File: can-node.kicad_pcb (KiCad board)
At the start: 2 copper layers, 50 x 60 mm, 96 parts, among them P1 Debug, P3 CONN_01X04, Q1 DMP6023LSS, Q10 BSS138, Q11 BSS84P, Q12 BSS84P, Q13 BSS84P, Q14 BSS84P, Q15 BSS84P, Q2 SFH3711, Q3 BSS138, Q4 BSS138, Q5 BSS138, Q6 BSS138, Q7 BSS138, Q8 BSS138, Q9 BSS138, SW1 SW_PUSH, SW2 SW_PUSH, SW3 SW_PUSH, U1 LMR16006, U2 SN74LVC1G08, U3 STM32F072RB, U4 HDC1080, U5 TCAN334, X1 32.768KHz 12.5pF

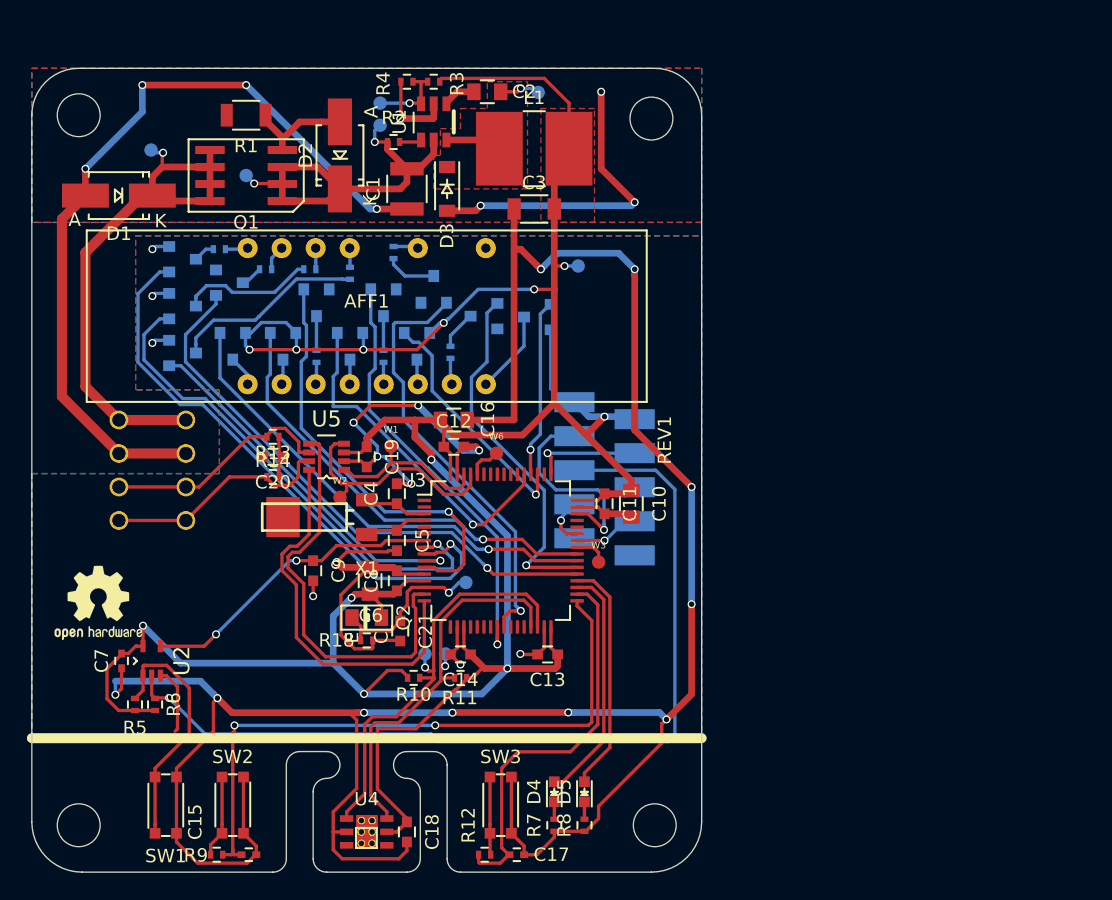
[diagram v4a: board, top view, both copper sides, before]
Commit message: Add 24V outputs.
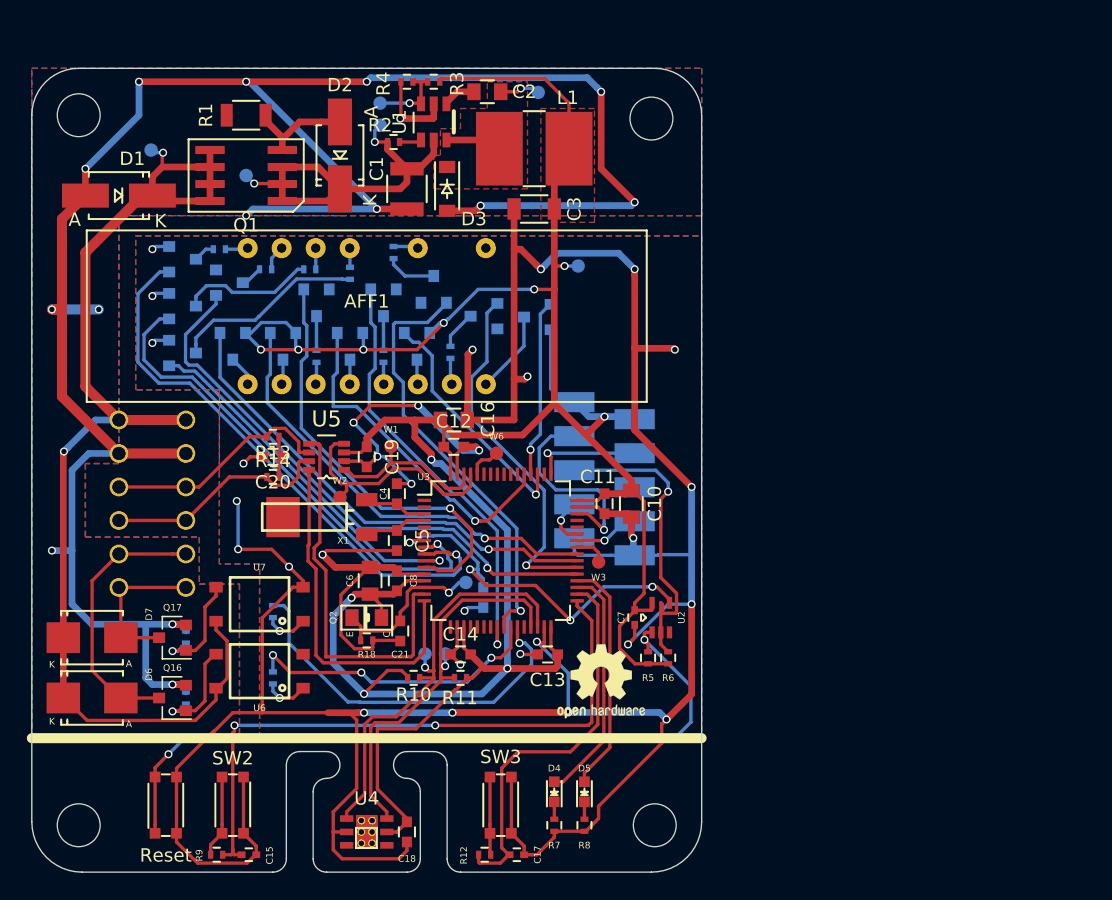
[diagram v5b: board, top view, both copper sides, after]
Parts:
- removed P3: CONN_01X04, CAN_Node:WAGO_218-104
- added D6: SM6T33A, Diodes_SMD:SMB_Standard, F.Cu at (124.5, 112.0)
- added D7: SM6T33A, Diodes_SMD:SMB_Standard, F.Cu at (124.5, 107.5)
- added P2: CONN_01X06, can-node:WAGO_218-106, B.Cu at (129.0, 97.5)
- added Q16: IRLML0060, TO_SOT_Packages_SMD:SOT-23, F.Cu at (130.5, 112.0)
- added Q17: IRLML0060, TO_SOT_Packages_SMD:SOT-23, F.Cu at (130.5, 107.5)
- added R15: 220, Resistors_SMD:R_0402, B.Cu at (138.0, 110.5)
- added R16: 10k, Resistors_SMD:R_0402, B.Cu at (131.5, 112.0)
- added R17: 220, Resistors_SMD:R_0402, B.Cu at (138.0, 105.5)
- added R19: 10k, Resistors_SMD:R_0402, B.Cu at (131.5, 107.5)
- added U6: LTV-356T, can-node:LTV356T, F.Cu at (137.0, 110.0)
- added U7: LTV-356T, can-node:LTV356T, F.Cu at (137.0, 105.0)
- C9: moved to B.Cu
- Q1: footprint CAN_Node:DMP6023LSS -> can-node:DMP6023LSS
- moved R6 38.5 mm to (167.5, 109.0)
- moved R5 38.5 mm to (166.0, 109.0)
- moved C7 38.4 mm to (165.0, 106.0)
- moved U2 38.1 mm to (166.9, 106.0)
- moved REF*** 38.0 mm to (162.5, 110.8)
- moved REF*** 26.5 mm to (163.3, 83.6)
- moved C9 12.9 mm to (153.7, 104.5)
- renumbered SW1 to Reset
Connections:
- net VIN renamed VIN+
- U3 pad 26: /Microcontroller/PB0 -> PB0
- U3 pad 27: /Microcontroller/PB1 -> PB1
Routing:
- net GND: track 339.1 -> 459.3 mm, vias 30 -> 45
- net Net-(P1-Pad5): track 68.7 -> 23.5 mm
- net VIN+: track 42.2 -> 85.0 mm, vias 1 -> 2
- net Net-(R5-Pad2): track 18.7 -> 56.0 mm, vias 0 -> 2
- net PB1: track 0.00 -> 28.4 mm, vias 0 -> 1
- net PB0: track 0.00 -> 22.4 mm, vias 0 -> 3
- net Net-(D6-Pad2): track 0.00 -> 20.4 mm
- net Net-(D7-Pad2): track 0.00 -> 11.7 mm
- net Net-(Q17-Pad1): track 0.00 -> 8.33 mm, vias 0 -> 1
- net Net-(Q16-Pad1): track 0.00 -> 7.87 mm, vias 0 -> 1
- net +3.3VADC: track 235.0 -> 227.3 mm, vias 12 -> 11
- net Net-(C9-Pad1): track 23.0 -> 28.1 mm, vias 2 -> 4
- net Net-(R15-Pad1): track 0.00 -> 3.31 mm, vias 0 -> 1
- net Net-(R17-Pad1): track 0.00 -> 3.26 mm, vias 0 -> 1
- net /Microcontroller/PA2: track 28.7 -> 26.6 mm
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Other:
- board text added: "OUT1"
- board text added: "OUT2"
- board text added: "VIN+/24V DC"
- board text added: "VIN-/0V"
- board text added: "designed with KiCAD"
- board text removed: "0V"
- board text removed: "24V DC"

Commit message: Remove unnecessary 24V out, minor changes.
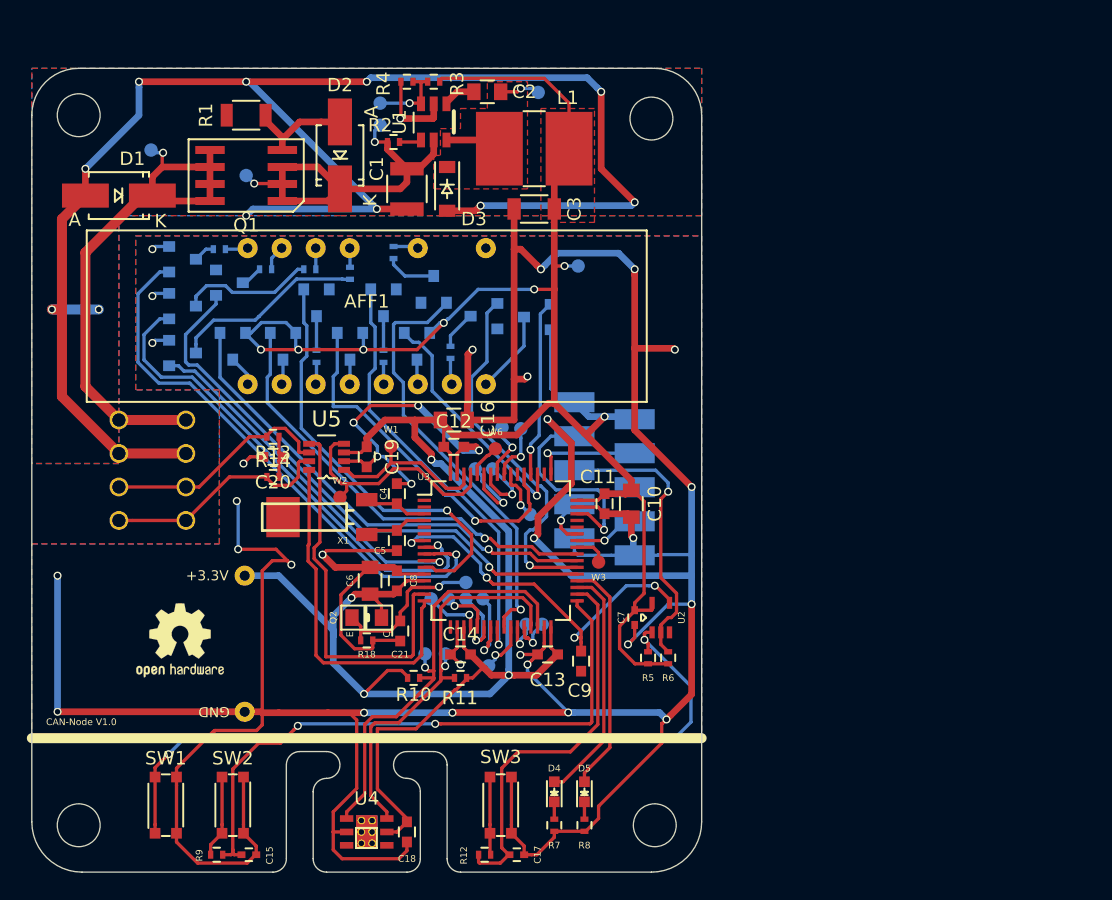
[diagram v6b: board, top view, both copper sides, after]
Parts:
- removed D6, D7: SM6T33A, Diodes_SMD:SMB_Standard
- removed Q16, Q17: IRLML0060, TO_SOT_Packages_SMD:SOT-23
- removed R15, R17: 220, Resistors_SMD:R_0402
- removed R16, R19: 10k, Resistors_SMD:R_0402
- removed Reset: SW_PUSH, CAN_Node:KMR2
- removed U6, U7: LTV-356T, can-node:LTV356T
- added SW1: SW_PUSH, can-node:KMR2, F.Cu at (130.0, 120.0)
- added W13: PA5, can-node:Measurement_Point_tiny, B.Cu at (151.1, 104.6)
- added W14: PA4, can-node:Measurement_Point_tiny, B.Cu at (149.8, 104.6)
- added W15: TEST_1P, can-node:TH-Pad_1.5mm, F.Cu at (135.9, 102.9)
- added W19: TEST_1P, can-node:TH-Pad_1.5mm, F.Cu at (135.9, 113.0)
- added W30: PB2, can-node:Measurement_Point_tiny, B.Cu at (158.1, 106.5)
- added W31: PB1, can-node:Measurement_Point_tiny, B.Cu at (156.9, 106.5)
- added W32: PB0, can-node:Measurement_Point_tiny, B.Cu at (154.1, 109.6)
- added W33: PB, can-node:Measurement_Point_tiny, B.Cu at (154.4, 94.9)
- added W34: PB, can-node:Measurement_Point_tiny, B.Cu at (155.1, 91.8)
- added W35: PB, can-node:Measurement_Point_tiny, B.Cu at (156.5, 91.9)
- added W36: PB, can-node:Measurement_Point_tiny, B.Cu at (157.2, 98.3)
- added W37: PB, can-node:Measurement_Point_tiny, B.Cu at (153.1, 94.9)
- added W4: PA7, can-node:Measurement_Point_tiny, B.Cu at (153.7, 104.6)
- added W5: PA6, can-node:Measurement_Point_tiny, B.Cu at (152.4, 104.6)
- C9: moved to F.Cu
- P2: value CONN_01X06 -> CONN_01X04; footprint can-node:WAGO_218-106 -> can-node:WAGO_218-104
- moved REF*** 31.6 mm to (131.1, 107.7)
- moved C9 8.71 mm to (161.0, 109.2)
- moved P2 2.50 mm to (129.0, 95.0)
- moved W6 0.34 mm to (154.6, 93.4)
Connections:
- U3 pad 26: PB0 -> /Microcontroller/PB0
- U3 pad 27: PB1 -> /Microcontroller/PB1
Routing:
- net VIN+: track 85.0 -> 42.2 mm, vias 2 -> 1
- net PB1: track 28.4 -> 0.00 mm, vias 1 -> 0
- net PB0: track 22.4 -> 0.00 mm, vias 3 -> 0
- net Net-(D6-Pad2): track 20.4 -> 0.00 mm
- net GND: track 459.3 -> 472.2 mm
- net Net-(D7-Pad2): track 11.7 -> 0.00 mm
- net +3.3VADC: track 227.3 -> 236.3 mm
- net Net-(Q17-Pad1): track 8.33 -> 0.00 mm, vias 1 -> 0
- net Net-(Q16-Pad1): track 7.87 -> 0.00 mm, vias 1 -> 0
- net Net-(U3-Pad22): track 0.00 -> 7.25 mm, vias 0 -> 1
- net /Microcontroller/PB7: track 0.00 -> 6.37 mm, vias 0 -> 1
- net Net-(U3-Pad23): track 0.00 -> 6.14 mm, vias 0 -> 1
- net /Microcontroller/PB6: track 0.00 -> 5.17 mm, vias 0 -> 1
- net /Microcontroller/PB4: track 0.00 -> 4.30 mm, vias 0 -> 1
- net Net-(U3-Pad20): track 0.00 -> 4.30 mm, vias 0 -> 1
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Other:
- board text added: "+3.3V"
- board text added: "CAN-Node V1.0"
- board text added: "GND"
- board text removed: "OUT1"
- board text removed: "OUT2"

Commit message: .
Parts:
- removed the REF*** at (163.3, 83.6)
- moved W2 6.00 mm to (141.2, 91.3)
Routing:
- net Net-(U3-Pad61): track 17.4 -> 18.5 mm
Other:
- board text added: "3.3V"
- board text added: "SWCLK"
- board text added: "SWDIO"
- board text added: "U_TX"
- board text removed: "REV1"
